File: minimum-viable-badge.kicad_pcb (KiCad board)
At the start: 2 copper layers, 100 x 100 mm, 62 parts, among them P1 BATTERY, P10 T4, P11 T0, P12 T1, P13 OLED_SPI, P2 USB, P6 T7, P7 T6, P9 T5, Q1 S8050, Q2 S8050, Q3 FDN340P, Q4 FDN340P, SW1 PRGM, SW2 RESET, SW3 ON|OFF, U1 CP2102, U2 ESP32-WROOM, U3 NCP5501, U4 CN3063, U5 MCP6002

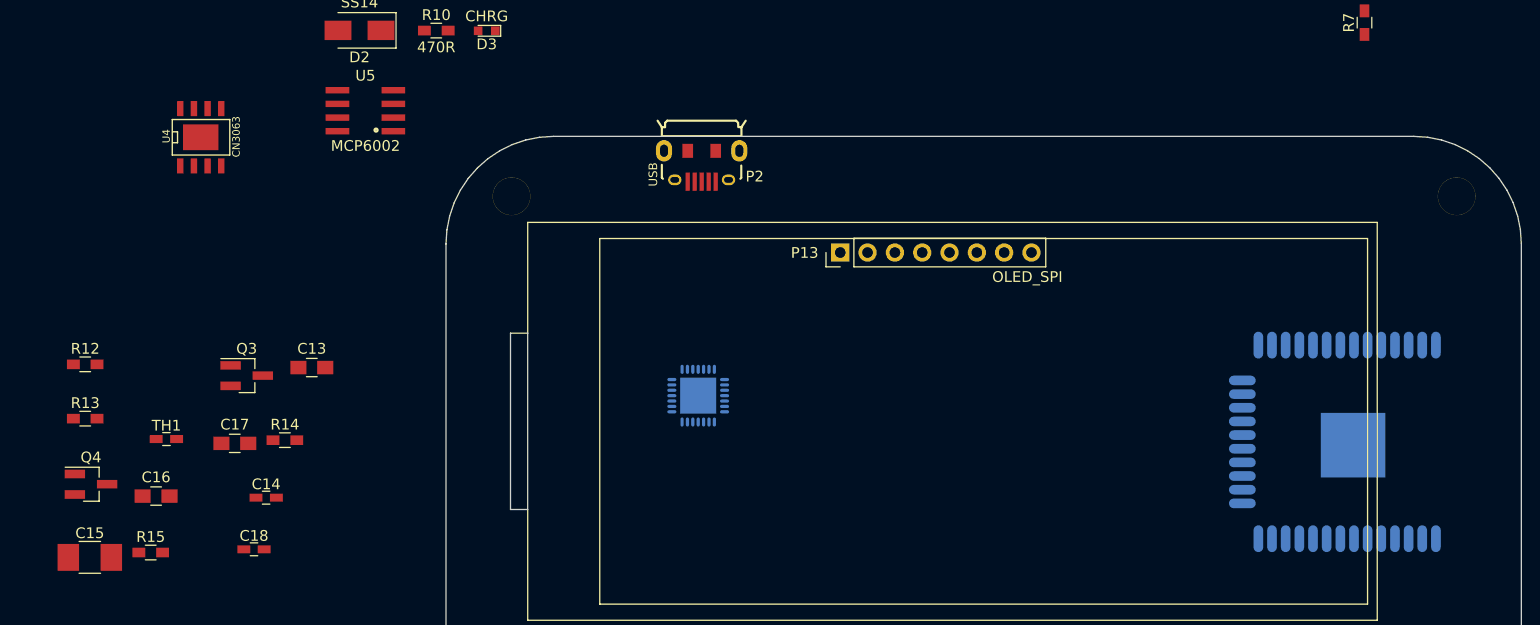
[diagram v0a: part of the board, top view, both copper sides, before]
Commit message: Now with less Hipster :(
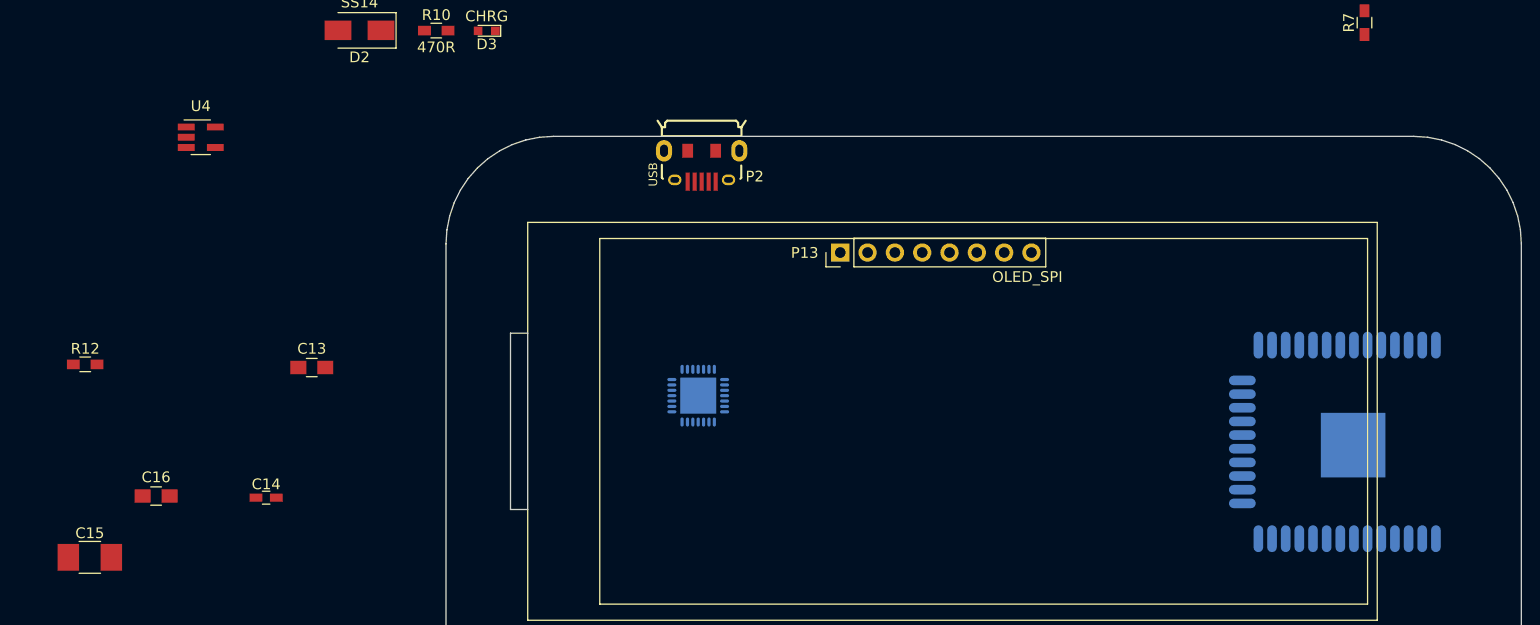
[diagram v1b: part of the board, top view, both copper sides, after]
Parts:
- removed C17: 10uF, Capacitors_SMD:C_0805_HandSoldering
- removed C18: 0.1uF, Capacitors_SMD:C_0603_HandSoldering
- removed Q3, Q4: FDN340P, TO_SOT_Packages_SMD:SOT-23_Handsoldering
- removed R13: 3.6K (1%), Resistors_SMD:R_0603_HandSoldering
- removed R14, R15: 100K, Resistors_SMD:R_0603_HandSoldering
- removed REF** (x2): 3.5mm, Mounting_Holes:MountingHole_3.5mm
- removed TH1: 10K NTC, Capacitors_SMD:C_0603_HandSoldering
- removed U5: MCP6002, libs:SO08_4mm
- C13, C16: value 10uF -> 4u7
- R12: value 3.6K (1%) -> 2K
- U4: value CN3063 -> MCP73831; footprint libs:CN3063_SOIC8_EP -> TO_SOT_Packages_SMD:SOT-23-5_HandSoldering
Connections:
- D3 pad 2: Net-(D3-Pad2) -> Net-(C13-Pad1)
- R10 pad 1: Net-(C13-Pad1) -> Net-(R10-Pad1)
- R10 pad 2: Net-(D3-Pad2) -> Net-(D3-Pad1)
- SW3 pad 1: /hipster-power/3.3V -> /BAT+
- U4 pad 1: Net-(R13-Pad2) -> Net-(R10-Pad1)
- U4 pad 2: Net-(R12-Pad1) -> GND
- U4 pad 3: GND -> /BAT+
- U4 pad 5: /BAT+ -> Net-(R12-Pad1)

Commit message: Updated cap sense.
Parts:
- removed C10, C5, C6, C7, C8, C9: C, Capacitors_SMD:C_0603_HandSoldering
- removed P11: T0, libs:button_round
- removed P12: T1, libs:button_round
- removed P13: OLED_SPI, Pin_Headers:Pin_Header_Straight_1x08_Pitch2.54mm
- removed SW1: PRGM, Buttons_Switches_ThroughHole:SW_PUSH_SMALL
- removed SW2: RESET, Buttons_Switches_ThroughHole:SW_PUSH_SMALL
- added R13: 100, Resistors_SMD:R_0603_HandSoldering, F.Cu at (233.1, 158.2)
- added R14: 100, Resistors_SMD:R_0603_HandSoldering, F.Cu at (237.7, 149.1)
- added R16: 100, Resistors_SMD:R_0603_HandSoldering, F.Cu at (233.2, 149.1)
- added R17: 100, Resistors_SMD:R_0603_HandSoldering, F.Cu at (237.9, 153.6)
- added R18: 100, Resistors_SMD:R_0603_HandSoldering, F.Cu at (237.9, 158.4)
- added R20: 100, Resistors_SMD:R_0603_HandSoldering, F.Cu at (233.2, 153.6)
- P10: value T4 -> POT_4; footprint libs:button_arrow -> libs:sense_pot
- P6: value T7 -> POT_1; footprint libs:button_arrow -> libs:sense_pot
- P7: value T6 -> POT_2; footprint libs:button_arrow -> libs:sense_pot
- P9: value T5 -> POT_3; footprint libs:button_arrow -> libs:sense_pot
- moved P10 88.6 mm to (156.8, 181.7), turned to 0 degrees
- moved P9 78.8 mm to (156.6, 171.2), turned to 0 degrees
- moved P7 59.6 mm to (156.5, 160.2), turned to 0 degrees
- moved U2 56.3 mm to (266.1, 15.4)
- moved P6 53.6 mm to (156.2, 150.1)
- moved U1 39.0 mm to (215.9, 31.6)
- moved P1 20.0 mm to (165.2, 115.1)
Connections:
- P10 pad 1: /IO15 -> Net-(P10-Pad1)
- P6 pad 1: /IO4 -> Net-(P6-Pad1)
- P7 pad 1: /IO0 -> Net-(P6-Pad2)
- P9 pad 1: /IO2 -> Net-(P9-Pad1)
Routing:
- net /IO4: track 48.5 -> 0.00 mm
- net /IO2: track 24.5 -> 0.00 mm
- net /IO0: track 23.4 -> 0.00 mm
- net /IO13: track 18.9 -> 0.00 mm
- net /IO12: track 18.9 -> 0.00 mm
- net /IO15: track 11.4 -> 0.00 mm

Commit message: Minor changes to the pcb.
Still testing ideas.
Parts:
- U3: moved to B.Cu
- moved D4 164.6 mm to (275.5, 29.8)
- moved R11 163.4 mm to (267.1, 25.9)
- moved SW3 160.7 mm to (272.6, 58.8), turned to 270 degrees
- moved U3 145.9 mm to (259.5, 50.7), turned to 270 degrees
- moved P7 135.1 mm to (237.5, 52.1)
- moved P10 116.4 mm to (237.8, 98.1)
- moved P6 114.2 mm to (214.9, 52.1)
- moved P9 93.6 mm to (215.1, 98.1)
- moved P2 77.2 mm to (274.4, 68.5), turned to 180 degrees
- moved U2 68.6 mm to (264.0, 83.9)
- moved P1 57.8 mm to (178.9, 59.0), turned to 270 degrees
- moved U1 52.4 mm to (258.4, 62.4)
- moved R7 18.1 mm to (244.2, 32.4)
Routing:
- net Net-(SW3-Pad2): track 25.1 -> 0.00 mm
- net +3V3: track 4.01 -> 0.00 mm
- net Net-(D4-Pad2): track 2.90 -> 0.00 mm
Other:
- outline, holes or cut-outs redrawn

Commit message: More pcb work
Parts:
- added P11: MECH, Mounting_Holes:MountingHole_3.2mm_M3_Pad, F.Cu at (182.4, 49.2)
- added P12: MECH, Mounting_Holes:MountingHole_3.2mm_M3_Pad, F.Cu at (271.1, 48.9)
- added P13: MECH, Mounting_Holes:MountingHole_3.2mm_M3_Pad, F.Cu at (182.4, 101.6)
- added P4: eInk, libs:FPC_0.5mm_Pitch_24_Pin, F.Cu at (198.0, 74.7)
- C1: footprint Capacitors_SMD:C_0603_HandSoldering -> Capacitors_SMD:C_0805_HandSoldering
- D3, D4, P10, P2, P6, P7, P9, SW3: moved to B.Cu
- P1, U1, U2, U3: moved to F.Cu
- moved Q1 210.8 mm to (258.6, 105.4)
- moved R2 198.8 mm to (263.1, 35.3)
- moved R5 191.7 mm to (267.5, 35.3)
- moved C3 181.1 mm to (269.5, 98.6), turned to 180 degrees
- moved R6 171.0 mm to (265.2, 87.6)
- moved R1 165.2 mm to (258.8, 35.3), turned to 180 degrees
- moved D1 164.8 mm to (194.1, 51.8)
- moved C1 163.5 mm to (261.9, 99.1)
- moved C2 160.9 mm to (261.9, 94.5)
- moved C4 159.0 mm to (269.5, 102.9), turned to 180 degrees
- moved R4 156.0 mm to (250.7, 104.4), turned to 180 degrees
- moved R3 148.0 mm to (249.2, 96.5), turned to 180 degrees
- moved Q2 147.3 mm to (255.8, 97.5)
- moved R13 146.5 mm to (198.9, 15.7), turned to 180 degrees
- moved R16 136.3 mm to (259.1, 15.2), turned to 180 degrees
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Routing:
- net +3V3: track 0.00 -> 176.9 mm, vias 0 -> 2
- net /USB_D+: track 0.00 -> 90.1 mm, vias 0 -> 1
- net /USB_D-: track 0.00 -> 90.0 mm, vias 0 -> 1
- net /USB_VCC: track 0.00 -> 84.5 mm, vias 0 -> 1
- net /DTR: track 0.00 -> 76.3 mm, vias 0 -> 2
- net /IO32: track 0.00 -> 72.5 mm
- net /IO33: track 0.00 -> 71.0 mm
- net /D/C: track 0.00 -> 69.2 mm
- net /IO26: track 0.00 -> 67.4 mm
- net /CS: track 0.00 -> 65.9 mm
- net Net-(SW3-Pad2): track 0.00 -> 63.1 mm
- net /RTS: track 0.00 -> 56.2 mm
- net /EN: track 0.00 -> 51.0 mm, vias 0 -> 2
- net /BAT+: track 0.00 -> 45.5 mm
- net Net-(F1-Pad1): track 0.00 -> 29.4 mm
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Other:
- board size 100 x 100 mm -> 100 x 66 mm

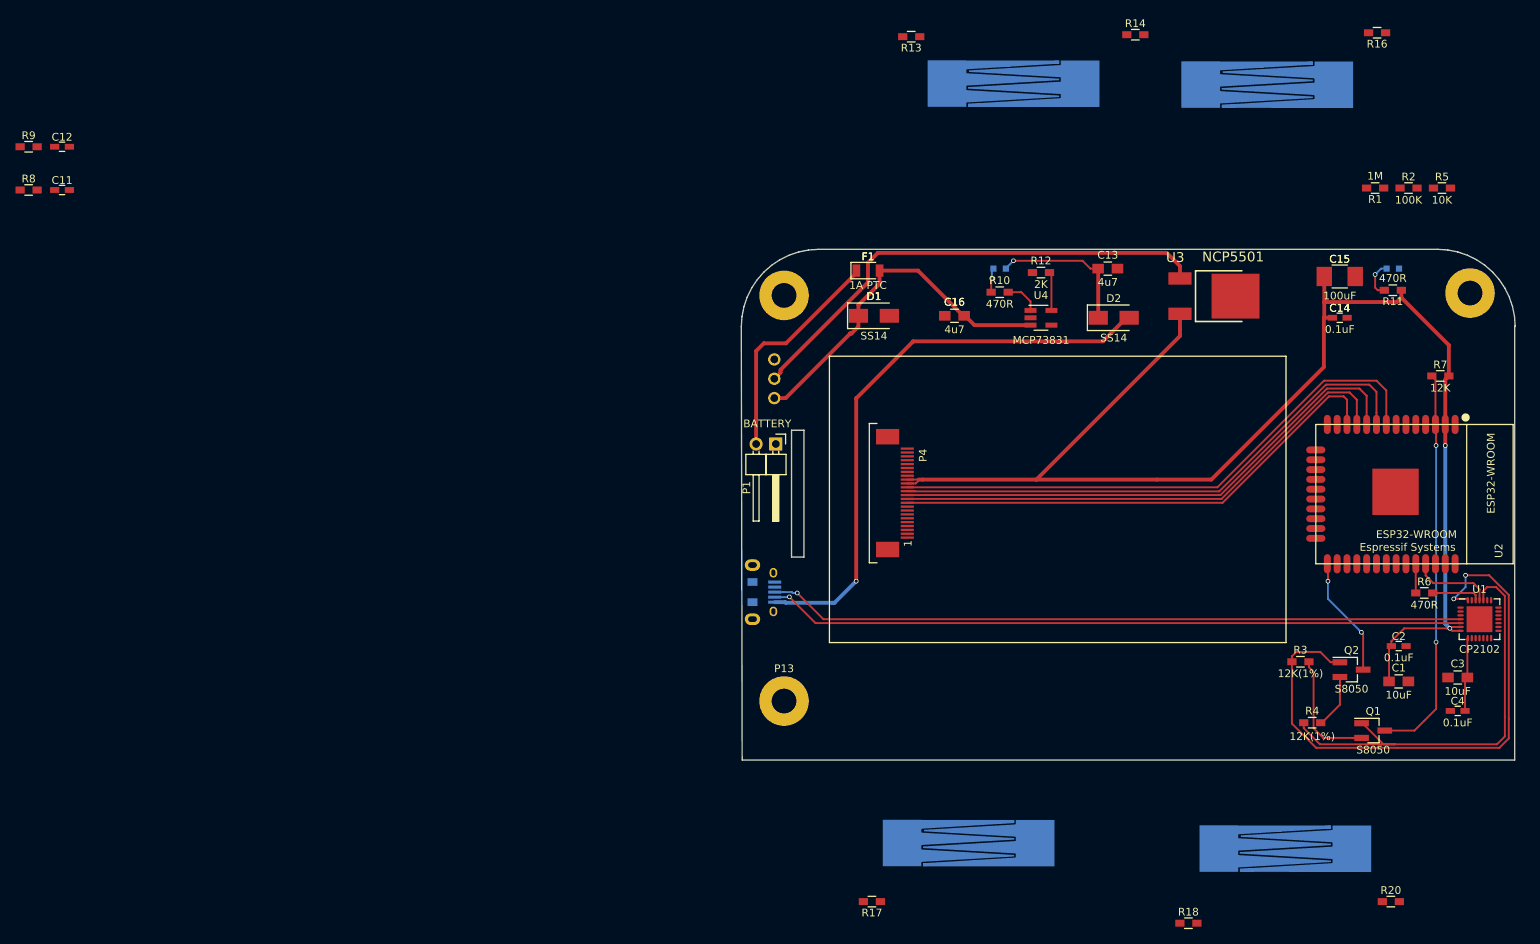
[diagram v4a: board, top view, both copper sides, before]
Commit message: Updated pcb layout.
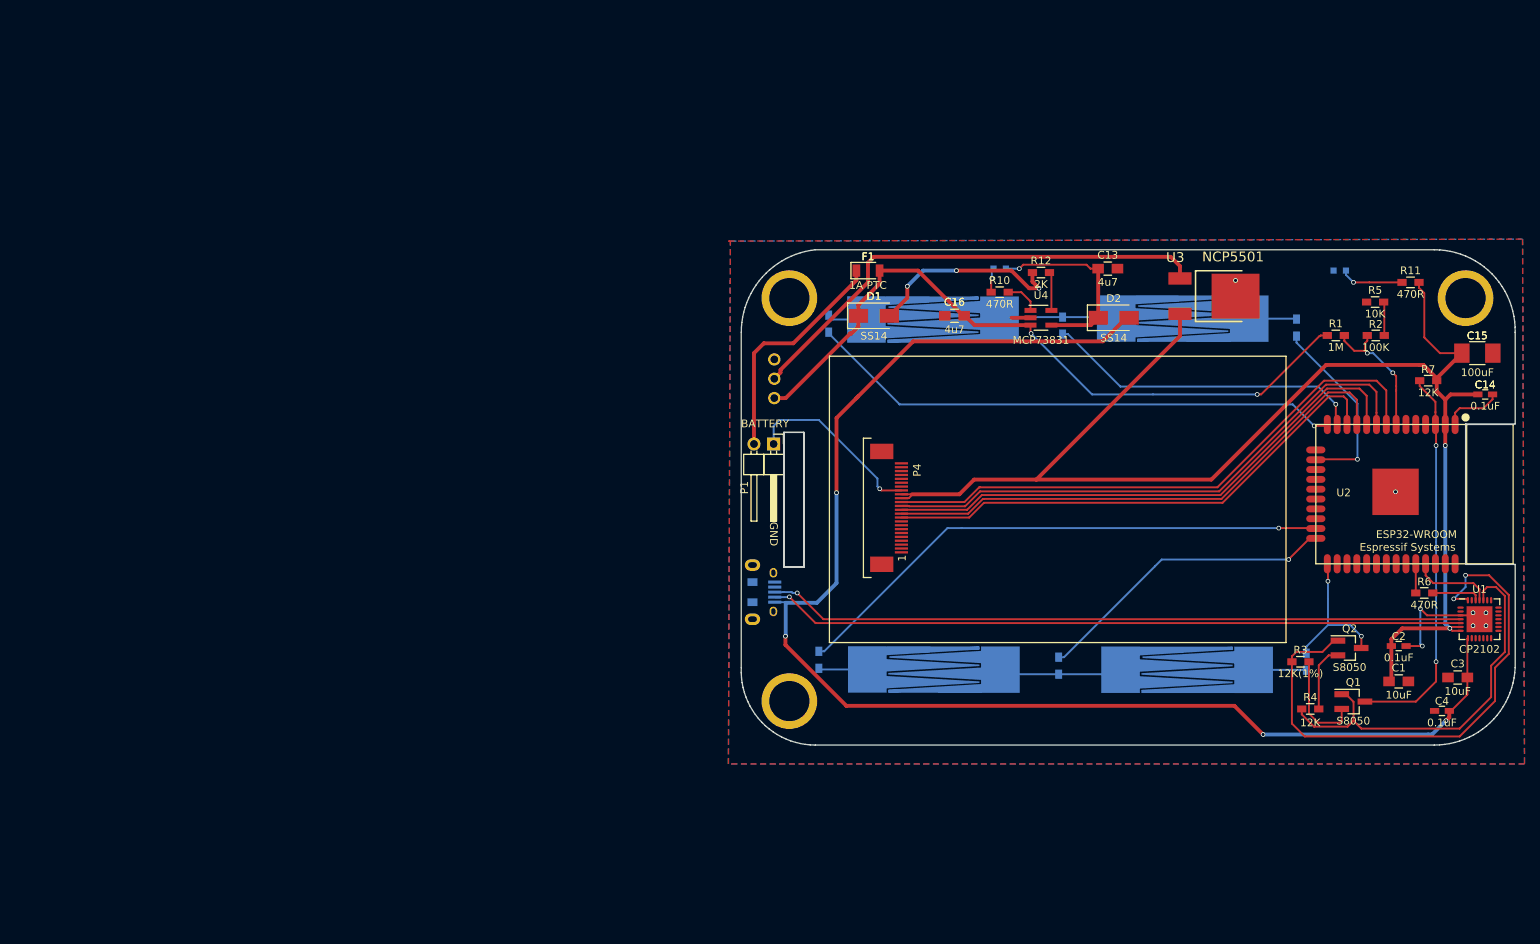
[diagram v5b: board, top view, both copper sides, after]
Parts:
- removed C11, C12: 1uF, Capacitors_SMD:C_0603_HandSoldering
- removed R8, R9: 470R, Resistors_SMD:R_0603_HandSoldering
- R13, R14, R16, R17, R18, R20: moved to B.Cu
- R4: value 12K(1%) -> 12K
- moved R16 39.5 mm to (248.7, 53.3), turned to 90 degrees
- moved R14 38.7 mm to (218.4, 53.1), turned to 90 degrees
- moved R13 38.6 mm to (188.2, 52.8), turned to 90 degrees
- moved R18 37.3 mm to (217.9, 97.0), turned to 270 degrees
- moved R20 32.9 mm to (249.9, 96.5), turned to 270 degrees
- moved P6 32.2 mm to (201.5, 52.3)
- moved P7 32.1 mm to (233.7, 52.2)
- moved R17 32.0 mm to (186.9, 96.3), turned to 270 degrees
- moved P10 26.4 mm to (234.3, 97.6)
- moved P9 22.9 mm to (201.6, 97.5)
- moved C14 21.2 mm to (273.1, 62.0)
- moved C15 20.4 mm to (272.0, 56.6)
- moved R1 19.7 mm to (253.7, 54.4)
- moved R2 19.5 mm to (258.9, 54.4)
- moved R5 17.1 mm to (258.8, 50.0), turned to 180 degrees
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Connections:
- R13 pad 1: /IO14 -> /IO12
- R14 pad 1: /IO12 -> /IO14
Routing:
- net /USB_VCC: track 84.5 -> 182.7 mm, vias 1 -> 4
- net GND: track 0.00 -> 74.6 mm, vias 0 -> 12
- net /IO15: track 0.00 -> 70.8 mm, vias 0 -> 1
- net Net-(P6-Pad2): track 0.00 -> 70.6 mm
- net /IO12: track 0.00 -> 69.6 mm, vias 0 -> 1
- net Net-(P10-Pad1): track 0.00 -> 68.3 mm
- net /BAT+: track 45.5 -> 91.3 mm, vias 0 -> 2
- net /IO14: track 0.00 -> 41.7 mm, vias 0 -> 1
- net /IO2: track 0.00 -> 39.7 mm, vias 0 -> 1
- net Net-(P10-Pad2): track 0.00 -> 34.3 mm
- net Net-(P7-Pad2): track 0.00 -> 33.6 mm
- net Net-(P9-Pad1): track 0.00 -> 30.9 mm
- net Net-(P6-Pad1): track 0.00 -> 29.7 mm
- net /IO13: track 0.00 -> 24.6 mm, vias 0 -> 1
- net /BAT_V: track 0.00 -> 17.8 mm, vias 0 -> 2
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- added copper zone on B.Cu, net GND
- added copper zone on F.Cu, net GND
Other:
- board size 100 x 66 mm -> 100 x 64 mm
- board text added: "GND"
- board text added: "https://github.com/mage0r/Minimum-viable-badge"

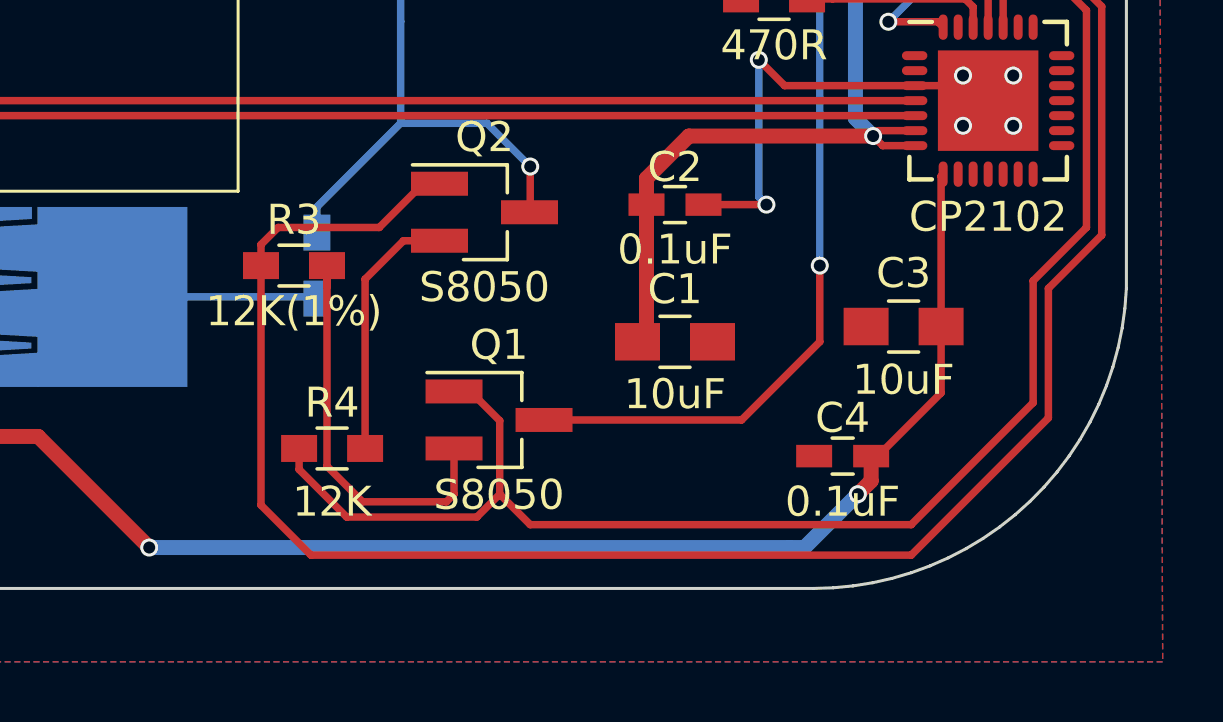
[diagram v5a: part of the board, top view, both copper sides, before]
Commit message: Damnit.  S8050 backwards
Thanks https://github.com/rdpowers.  Fixes #2
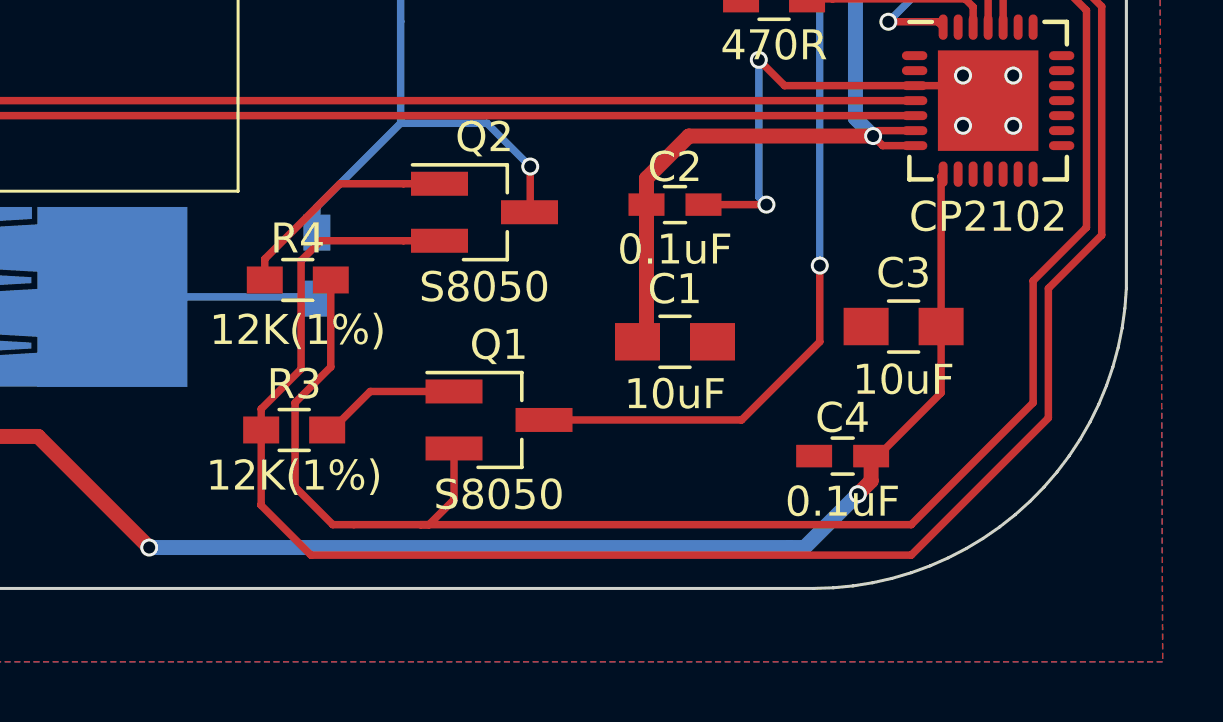
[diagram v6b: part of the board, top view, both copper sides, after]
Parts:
- R4: value 12K -> 12K(1%)
- moved R4 5.73 mm to (249.3, 97.0), turned to 0 degrees
- moved R3 5.48 mm to (249.2, 102.0)
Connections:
- Q1 pad 1: /RTS -> Net-(Q1-Pad1)
- Q1 pad 2: Net-(Q1-Pad2) -> /RTS
- Q2 pad 1: /DTR -> Net-(Q2-Pad1)
- Q2 pad 2: Net-(Q2-Pad2) -> /DTR
- R3 pad 1: Net-(Q1-Pad2) -> Net-(Q1-Pad1)
- R4 pad 1: Net-(Q2-Pad2) -> Net-(Q2-Pad1)
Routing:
- net Net-(Q1-Pad2): track 13.7 -> 0.00 mm
- net Net-(Q2-Pad2): track 8.65 -> 0.00 mm
- net Net-(Q2-Pad1): track 0.00 -> 8.38 mm
- net Net-(Q1-Pad1): track 0.00 -> 5.86 mm
- net /RTS: track 51.1 -> 55.9 mm
- net /DTR: track 71.0 -> 69.6 mm
